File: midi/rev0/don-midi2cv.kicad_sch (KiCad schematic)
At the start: 112 parts, among them J1 DIN-5_180degree, J10 CV1, J11 CV2, J12 VEL1, J13 VEL2, J2 Conn_02x03_Odd_Even, J3 Conn_02x08_Odd_Even, J5 UART, J7 MIDICLK, J8 GATE1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

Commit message: Midi2CV component selection partly done
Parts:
- C10, C11, C6: PartID (none) -> CAP0020
- C2, C3, C4, C5: PartID (none) -> -
- J10, J11, J12, J13, J7, J8, J9, JP1, JP2, JP3, TP1, TP17, TP18, TP19, TP2, TP20, TP3, TP4, TP5, TP6, TP7: Digikey (none) -> -; LCSC (none) -> -
- RV1, RV2, RV3, RV4, RV5: Digikey (none) -> TC33X-202ECT-ND (etc); LCSC (none) -> C720647 / C720646 / C719174 / C720648 / C719176 / C911390; PartID (none) -> POT002?
- U1: Digikey (none) -> NCP1117ST33T3GOSCT-ND; LCSC (none) -> C26537
- U10: Digikey (none) -> 296-47739-1-ND; LCSC (none) -> C713689
- U2: Digikey (none) -> 497-14043-ND; LCSC (none) -> C23922
- U3: Digikey (none) -> 6N138SDMCT-ND; LCSC (none) -> C188666
- U4, U5, U8, U9: Digikey (none) -> 497-2200-1-ND; LCSC (none) -> C6962
- U6, U7: Digikey (none) -> MCP4922-E/SL-ND; LCSC (none) -> C39851
- Y1: Digikey (none) -> 535-9542-1-ND; LCSC (none) -> C655072
- Y2: Digikey (none) -> 3997-C3E-8.000-10-1020-MCT-ND; LCSC (none) -> C648985

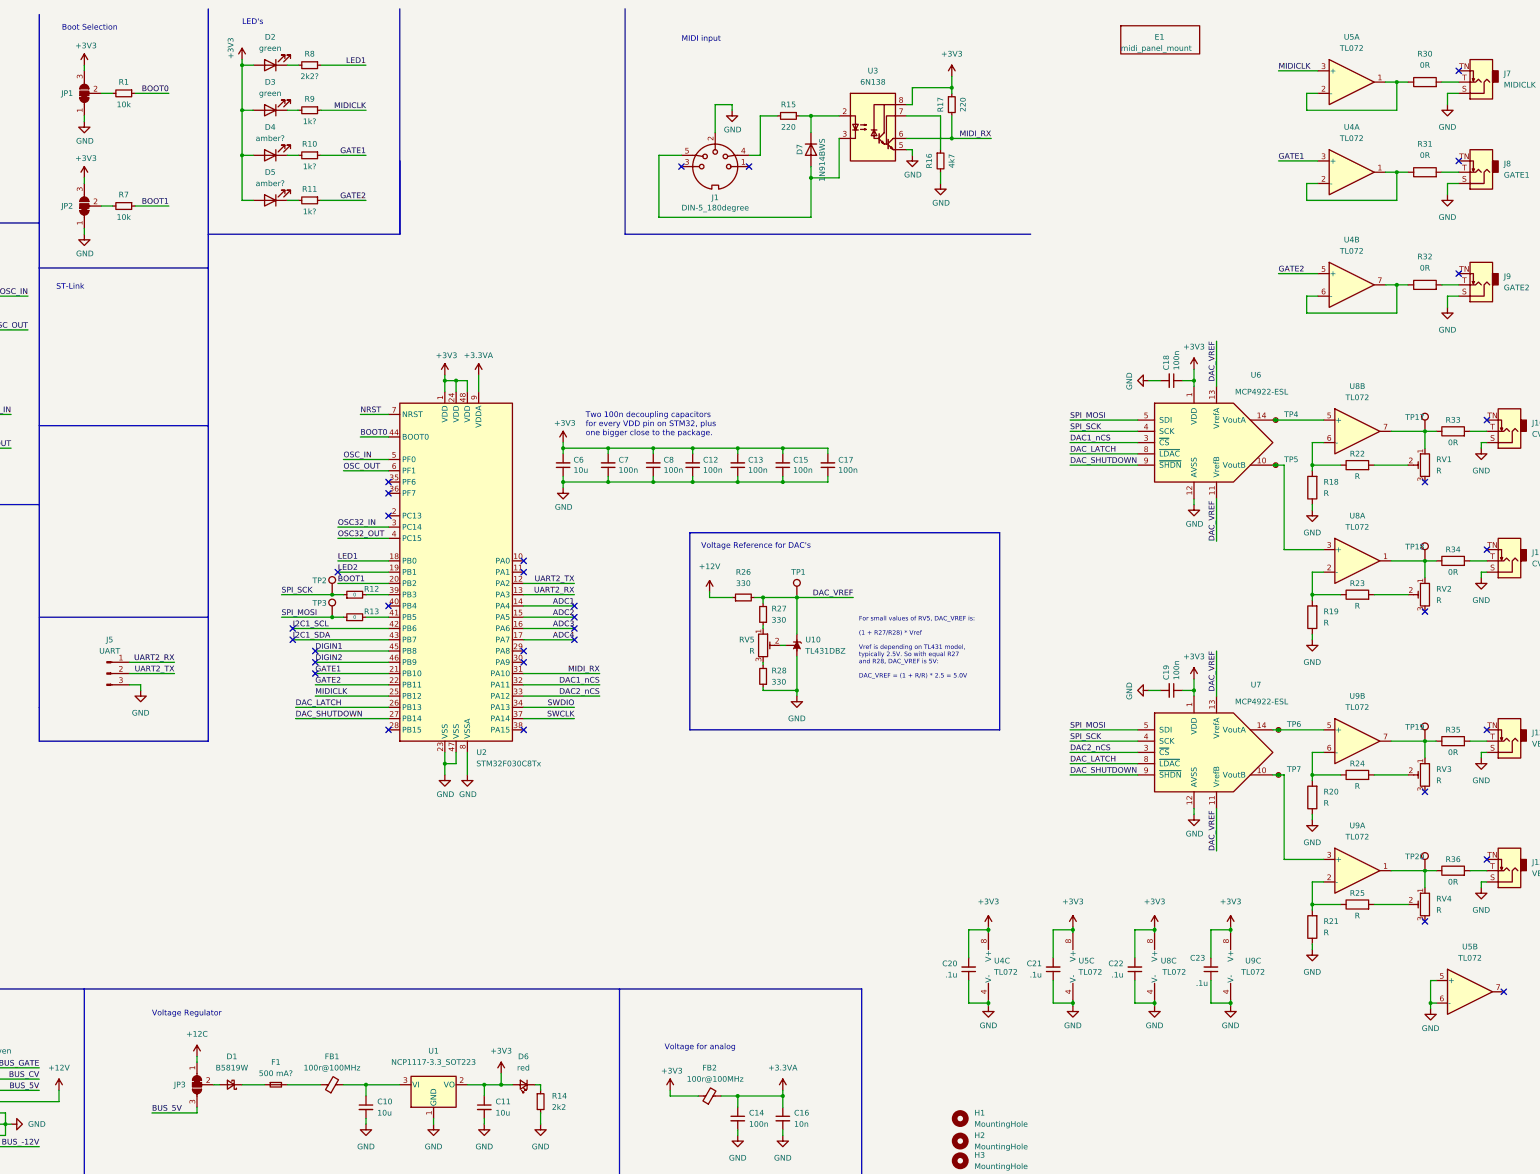
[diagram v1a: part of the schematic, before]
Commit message: midi2cv: completed bom selection and migrated to newer version of kicad
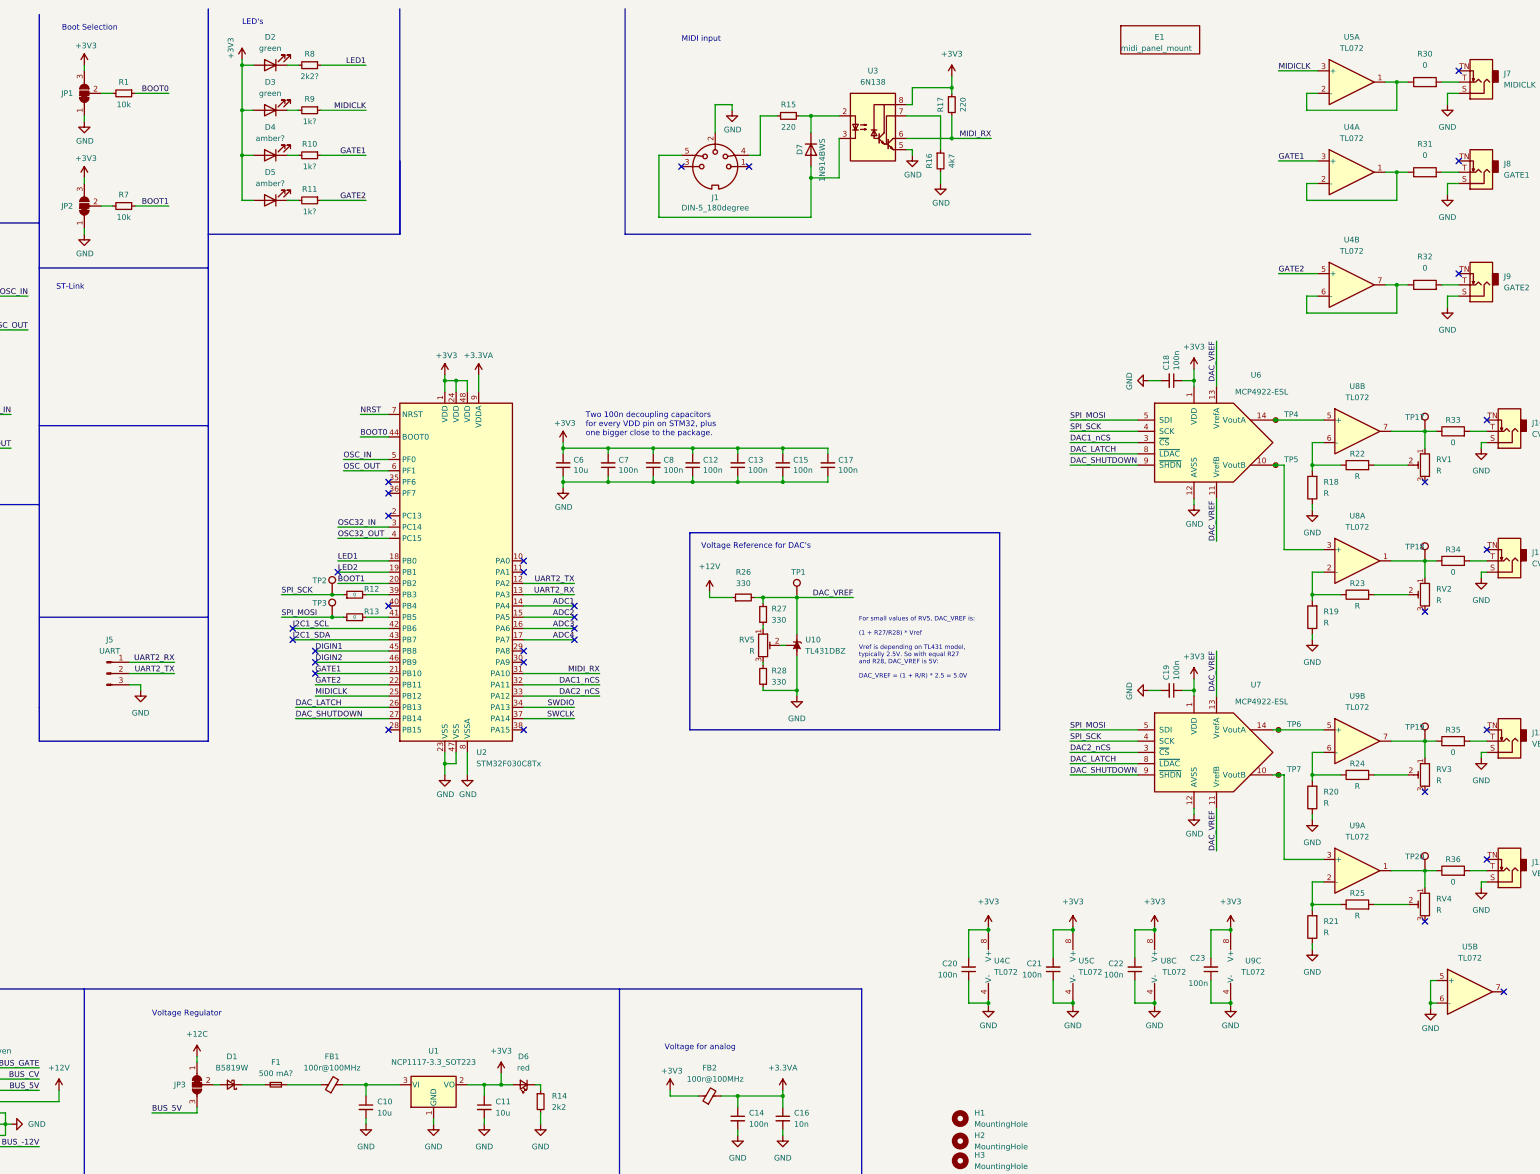
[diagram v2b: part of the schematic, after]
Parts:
- C1, C12, C13, C14, C15, C17, C18, C19, C7, C8: PartID (none) -> CAP0015
- C16: PartID (none) -> CAP0038
- C2, C3: LCSC (none) -> CC0603JRNPO9BN200
- C20, C21, C22, C23: value .1u -> 100n; PartID (none) -> CAP0015
- C4, C5: LCSC (none) -> CC0603JRNPO9BN100
- D1: LCSC (none) -> C2910056
- D2, D3: LCSC (none) -> C434423
- D4, D5: LCSC (none) -> C434425
- D6: LCSC (none) -> C434419
- D7: LCSC (none) -> C258181
- E1, H1, H2, H3, H4, J1: Digikey (none) -> -; LCSC (none) -> -; PartID (none) -> -
- F1: LCSC (none) -> C310922
- FB1, FB2: LCSC (none) -> -; PartID (none) -> skip for now?
- J2, J3, J5: Digikey (none) -> stock; LCSC (none) -> stock; PartID (none) -> stock
- R1, R3, R7: PartID (none) -> RES0011
- R10, R11, R9: PartID (none) -> RES0013
- R12, R13: PartID (none) -> RES0027
- R14, R8: LCSC (none) -> C114662; PartID (none) -> RES0038
- R15, R17: LCSC (none) -> C107696
- R16: PartID (none) -> RES0010
- R2: LCSC (none) -> C114620
- R26, R27, R28: LCSC (none) -> C105881
- R30, R31, R32, R33, R34, R35, R36: value 0R -> 0; PartID (none) -> RES0027
- SW1: LCSC (none) -> C393938
- U1: LCSC C26537 -> C146799 (or C26537)
- U3: LCSC C188666 -> C188666 or C3001991

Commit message: midi: first prototype populated
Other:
- note added: "TODO: - The optocoupler (U3) selected is through-hole (6N138) - Diode D7, by U3, is hard to solder. Change component or footprint. - Vref U10 footprint does not match component. Mirrored."
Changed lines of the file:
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@@
+    (effects (font (size 1.27 1.27)) (justify left bottom))
+  )
+  (text "TODO:\n\n- The optocoupler (U3) selected is through-hole (6N138)\n- Diode D7, by U3, is hard to solder. Change component or footprint.\n- Vref U10 footprint does not match component. Mirrored."
+    (at 203.2 78.74 0)
     (effects (font (size 1.27 1.27)) (justify left bottom))
   )
